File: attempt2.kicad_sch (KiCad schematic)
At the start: 70 parts, among them J1 SIM_Card, J3 U.FL-R-SMT-110, J4 USB_C_Receptacle_USB2.0_14P, J5 U.FL-R-SMT-110, SW3 SW_Push, SW4 SW_Push, U1 nRF9160-SIxA, U3 MCP73831T-2ACI_OT, U4 MIC94092YC6-TR, U7 CP2102N-A02-GQFN24R

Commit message: all the footprints...
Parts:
- BT1: footprint (none) -> PCB_schem_downloads:SEIKO_ML414H_IV01E
- C1, C10, C11, C12, C13, C14, C15, C16, C19, C4, C5, C6, C8, C9: footprint (none) -> Capacitor_SMD:C_1206_3216Metric
- D1, D3: footprint (none) -> LED_SMD:LED_1206_3216Metric
- D4: footprint BAT20JFILM:SOD-323 -> Diode_SMD:D_2114_3652Metric
- J1: footprint (none) -> Connector_Card:nanoSIM_GCT_SIM8060-6-1-14-00
- J3, J5: footprint CONN1_UFL-R_HIR -> footprints:CONN1_UFL-R_HIR
- J4: footprint (none) -> Connector_USB:USB_C_Receptacle_GCT_USB4110
- JP2: footprint (none) -> Jumper:SolderJumper-2_P1.3mm_Open_RoundedPad1.0x1.5mm
- L1, L4: footprint (none) -> Inductor_SMD:L_1206_3216Metric
- PS1: footprint TPS63031DSKR:SON50P250X250X80-11N -> Package_SON:WSON-10-1EP_2.5x2.5mm_P0.5mm_EP1.2x2mm
- R1, R10, R11, R12, R15, R16, R17, R2, R20, R21, R3, R4, R5, R6, R7, R8, R9: footprint (none) -> Resistor_SMD:R_1206_3216Metric
- SW3: footprint (none) -> Button_Switch_SMD:SW_Push_1P1T_NO_CK_PTS125Sx43PSMTR
- SW4: footprint (none) -> Button_Switch_SMD:SW_Push_1P1T_NO_CK_PTS125Sx73SMTR
- TP1, TP10, TP11, TP13, TP14, TP15, TP16, TP19, TP2, TP20, TP21, TP3, TP4, TP5, TP6, TP7, TP8, TP9: footprint (none) -> TestPoint:TestPoint_Pad_D2.0mm
- U3: footprint MCP73831T-2ACI_OT:SOT95P280X145-5N -> MCP73831T_2ACI_OT:SOT95P280X145-5N
- U4: footprint SC-70-6_C6_MCH -> footprints:SC-70-6_C6_MCH
- U7: footprint CP2102N-A02-GQFN24R:QFN50P400X400X80-25N -> CP2102N_A02_GQFN24R:QFN50P400X400X80-25N
- gave numbers to parts that had none: 1
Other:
- note added: "# TODO: ## bake - give mia the battery sense voltage divider values - antennae things ## mia - assign footprints :) all done except for sw pins - add notes about the expected voltage/current values for things (ie. buck/boost output, VBUS/VSYS lines, etc.) - route pcb"
- note added: "VBAT = (2.0, 3.0, 3.1)V 1.0mAh Battery: ML414H IV01E Coin Cell Battery"
- note added: "VBUS = 5.0V +-0.5v 48V DC 280W USB4110-GF-A"
- note added: "VSYS = (3.3, 3.3, 3.3)V VIN RANGE: 1.8-5.5V"
- note removed: "# TODO: ## bake - give mia the battery sense voltage divider values - antennae things ## mia - assign footprints :) - add notes about the expected voltage/current values for things (ie. buck/boost output, VBUS/VSYS lines, etc.) - route pcb"
- note removed: "VBAT = (3.0, 3.7, 4.2)V"
- note removed: "VBUS = 5.1V +-0.5v"

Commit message: started work on pcb
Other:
- note added: "VBAT = (3.0, 3.7, 4.2)V"
- note added: "VBUS = 5.1V +-0.5v"
- note removed: "VBAT = (2.0, 3.0, 3.1)V 1.0mAh Battery: ML414H IV01E Coin Cell Battery"
- note removed: "VBUS = 5.0V +-0.5v 48V DC 280W USB4110-GF-A"
- note removed: "VSYS = (3.3, 3.3, 3.3)V VIN RANGE: 1.8-5.5V"
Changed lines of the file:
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@@
 		)
 	)
-	(text "VBUS = 5.0V +-0.5v 48V DC 280W\nUSB4110-GF-A"
+	(text "VBUS = 5.1V +-0.5v"
 		(exclude_from_sim no)
-		(at 56.896 259.08 0)
+		(at 51.308 253.746 0)
 		(effects
 			(font
@@
 		)
 	)
-	(text "VBAT = (2.0, 3.0, 3.1)V 1.0mAh\nBattery: ML414H IV01E Coin Cell Battery\n"
+	(text "VBAT = (3.0, 3.7, 4.2)V"
 		(exclude_from_sim no)
 		(at 91.186 336.296 0)
@@
 			)
 		)
-	)
-	(text "VSYS = (3.3, 3.3, 3.3)V\nVIN RANGE: 1.8-5.5V\n"
-		(exclude_from_sim no)
-		(at 231.648 287.782 0)
-		(effects
-			(font
-				(size 1.27 1.27)
-			)
-		)

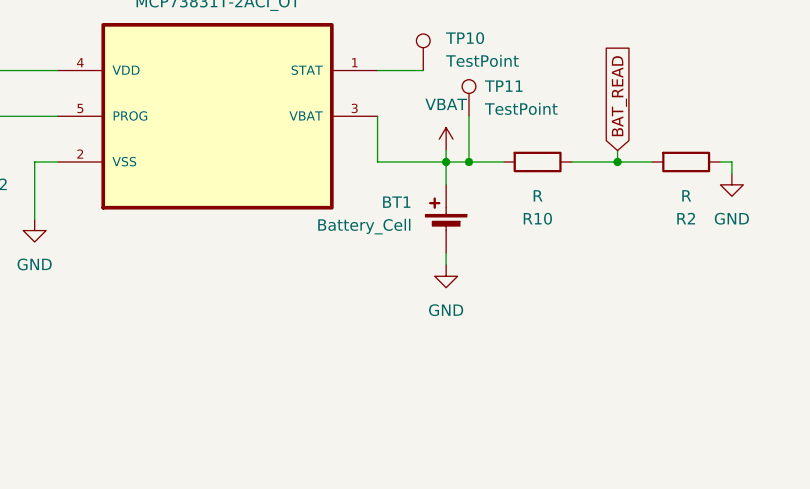
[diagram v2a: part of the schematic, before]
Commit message: added a diode
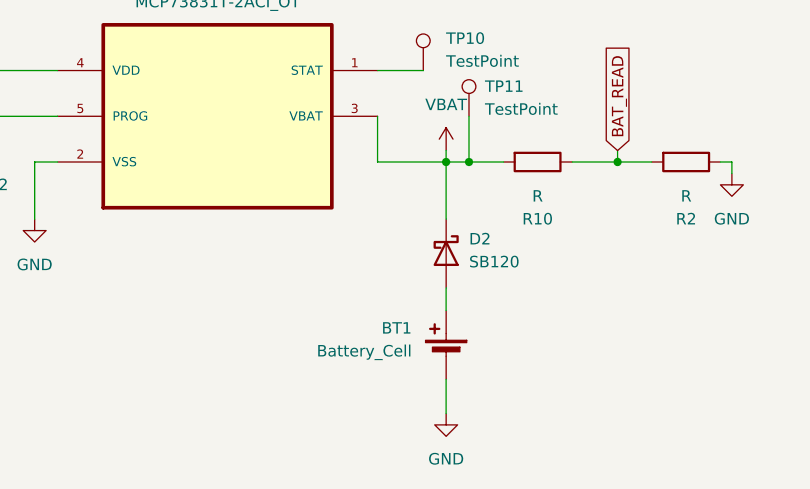
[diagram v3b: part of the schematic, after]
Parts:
- added D2: SB120, Diode_THT:D_DO-41_SOD81_P10.16mm_Horizontal, symbol Diode:SB120
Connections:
- net VBAT: now also D2.1 (K); no longer BT1.1 (+)
- new net: BT1.1 (+), D2.2 (A)
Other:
- moved on the sheet: BT1
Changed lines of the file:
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@@
 	(wire
 		(pts
+			(xy 115.57 373.38) (xy 115.57 367.03)
+		)
+		(stroke
+			(width 0)
+			(type default)
+		)
+	)
+	(wire
+		(pts
 			(xy 252.73 110.49) (xy 276.86 110.49)
 		)
@@
 	(wire
 		(pts
-			(xy 115.57 378.46) (xy 115.57 377.19)
+			(xy 115.57 391.16) (xy 115.57 394.97)
 		)
 		(stroke
@@
 	(wire
 		(pts
-			(xy 115.57 369.57) (xy 115.57 367.03)
+			(xy 115.57 383.54) (xy 115.57 381)
 		)
 		(stroke
@@
 	)
 	(symbol
+		(lib_id "Diode:SB120")
+		(at 115.57 377.19 270)
+		(unit 1)
+		(exclude_from_sim no)
+		(in_bom yes)
+		(on_board yes)
+		(dnp no)
+		(fields_autoplaced yes)
+		(property "Reference" "D2"
+			(at 118.11 375.6024 90)
+			(effects
+				(font
+					(size 1.27 1.27)
+				)
+				(justify left)
+			)
+		)
+		(property "Value" "SB120"
+			(at 118.11 378.1424 90)
+			(effects
+				(font
+					(size 1.27 1.27)
+				)
+				(justify left)
+			)
+		)
+		(property "Footprint" "Diode_THT:D_DO-41_SOD81_P10.16mm_Horizontal"
+			(at 111.125 377.19 0)
+			(effects
+				(font
+					(size 1.27 1.27)
+				)
+				(hide yes)
+			)
+		)
+		(property "Datasheet" "http://www.diodes.com/_files/datasheets/ds23022.pdf"
+			(at 115.57 377.19 0)
+			(effects
+				(font
+					(size 1.27 1.27)
+				)
+				(hide yes)
+			)
+		)
+		(property "Description" "20V 1A Schottky Barrier Rectifier Diode, DO-41"
+			(at 115.57 377.19 0)
+			(effects
+				(font
+					(size 1.27 1.27)
+				)
+				(hide yes)
+			)
+		)
+		(pin "2"
+		)
+		(pin "1"
+		)
+		(instances
+			(project ""
+				(path "/b2ea7ca0-f81a-4f8c-9e17-16fbc56b39ae"
+					(reference "D2")
+					(unit 1)
+				)
+			)
+		)
+	)
+	(symbol
 		(lib_id "Device:L")
 		(at 74.93 62.23 90)
@@
 	(symbol
 		(lib_id "power:GND")
-		(at 115.57 378.46 0)
+		(at 115.57 394.97 0)
 		(unit 1)
 		(exclude_from_sim no)
@@
 		(fields_autoplaced yes)
 		(property "Reference" "#PWR026"
-			(at 115.57 384.81 0)
+			(at 115.57 401.32 0)
 			(effects
 				(font
@@
 		)
 		(property "Value" "GND"
-			(at 115.57 383.54 0)
+			(at 115.57 400.05 0)
 			(effects
 				(font
@@
 		)
 		(property "Footprint" ""
-			(at 115.57 378.46 0)
+			(at 115.57 394.97 0)
 			(effects
 				(font
@@
 		)
 		(property "Datasheet" ""
-			(at 115.57 378.46 0)
+			(at 115.57 394.97 0)
 			(effects
 				(font
@@
 		)
 		(property "Description" "Power symbol creates a global label with name \"GND\" , ground"
-			(at 115.57 378.46 0)
+			(at 115.57 394.97 0)
 			(effects
 				(font
@@
 	(symbol
 		(lib_id "Device:Battery_Cell")
-		(at 115.57 374.65 0)
+		(at 115.57 388.62 0)
 		(mirror y)
 		(unit 1)
@@
 		(dnp no)
 		(property "Reference" "BT1"
-			(at 111.76 371.5384 0)
+			(at 111.76 385.5084 0)
 			(effects
 				(font
@@
 		)
 		(property "Value" "Battery_Cell"
-			(at 111.76 374.0784 0)
+			(at 111.76 388.0484 0)
 			(effects
 				(font
@@
 		)
 		(property "Footprint" "PCB_schem_downloads:SEIKO_ML414H_IV01E"
-			(at 115.57 373.126 90)
+			(at 115.57 387.096 90)
 			(effects
 				(font
@@
 		)
 		(property "Datasheet" "~"
-			(at 115.57 373.126 90)
+			(at 115.57 387.096 90)
 			(effects
 				(font
@@
 		)
 		(property "Description" "Single-cell battery"
-			(at 115.57 374.65 0)
+			(at 115.57 388.62 0)
 			(effects
 				(font

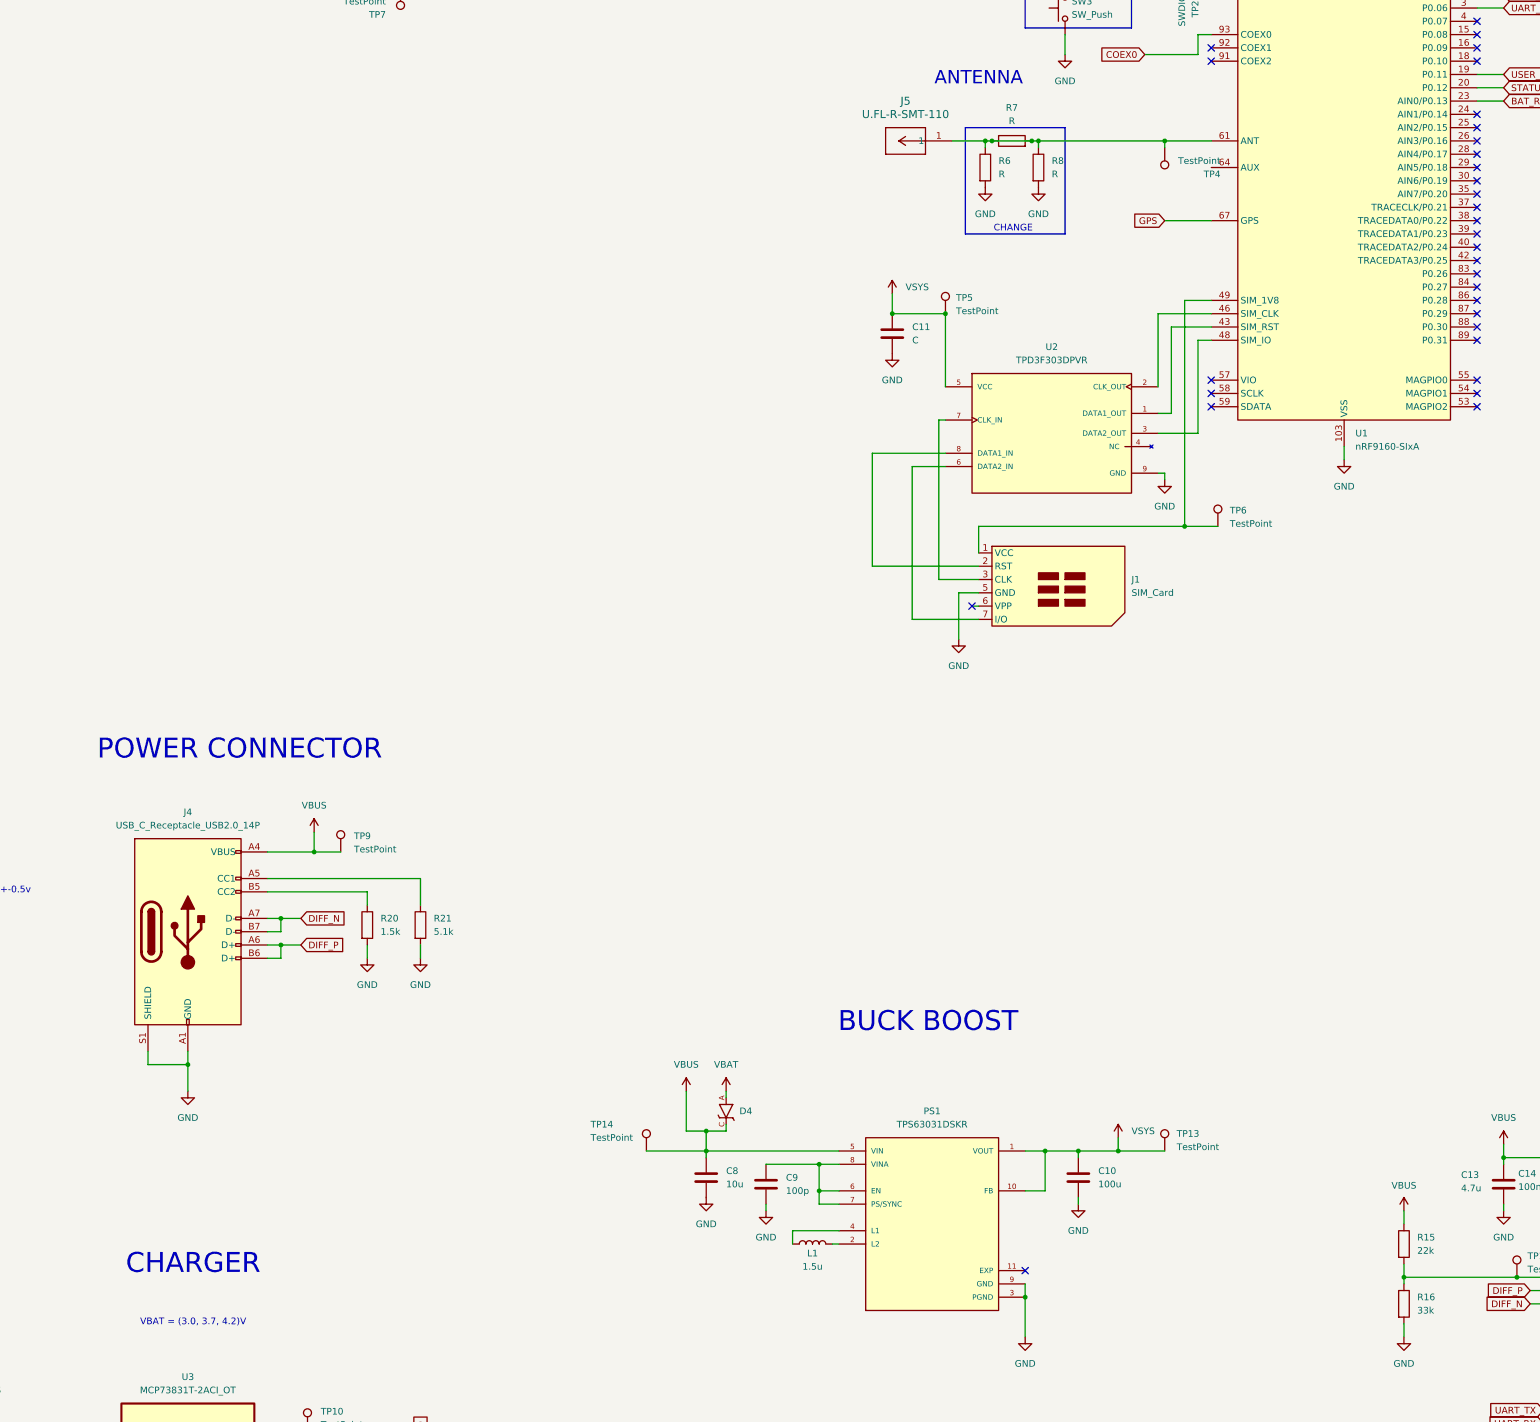
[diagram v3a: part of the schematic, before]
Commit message: changed out antenna and fixed jst battery connector. also edited schematic
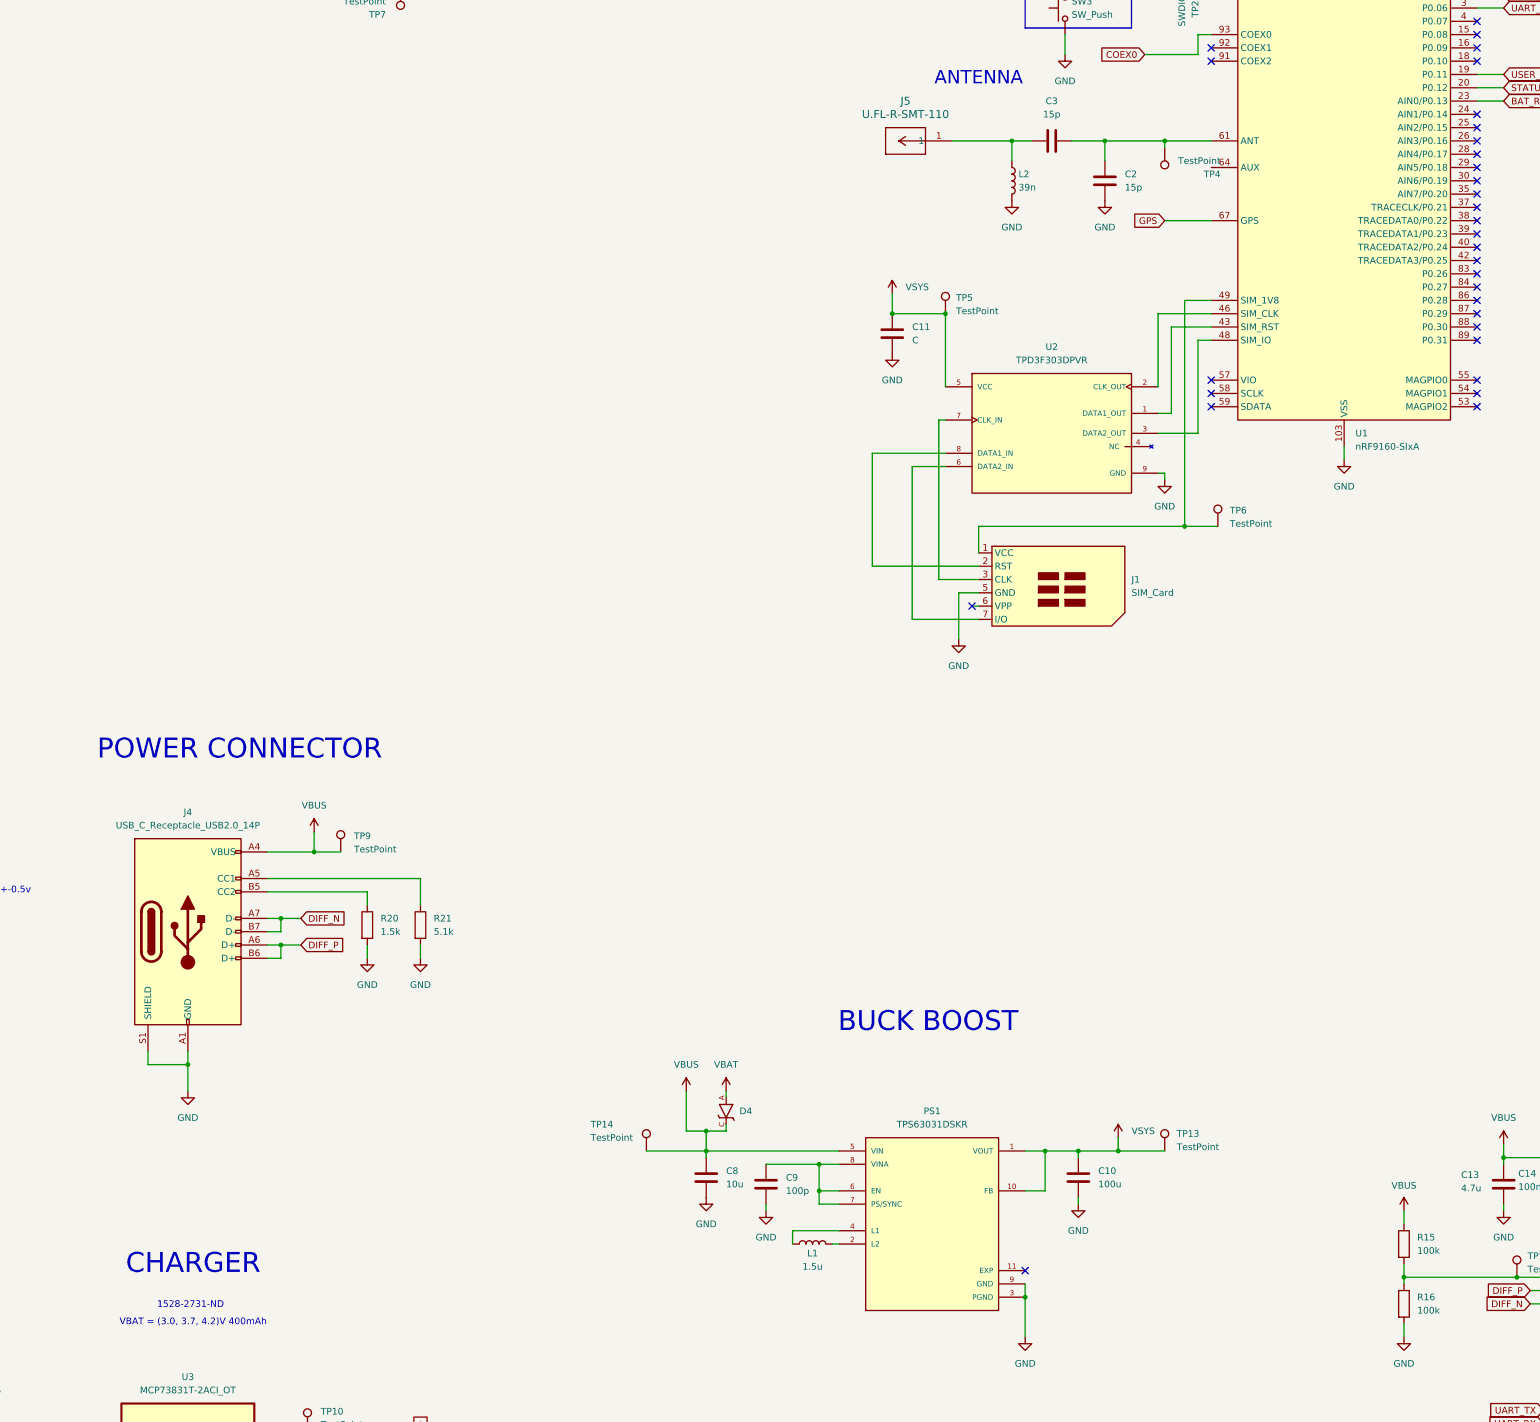
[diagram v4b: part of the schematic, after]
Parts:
- removed R6, R7, R8: R, Resistor_SMD:R_1206_3216Metric, symbol Device:R
- added C2, C3: 15p, Capacitor_SMD:C_1206_3216Metric, symbol Device:C
- added L2: 39n, Inductor_SMD:L_1206_3216Metric, symbol Device:L
- BT1: footprint PCB_schem_downloads:SEIKO_ML414H_IV01E -> Connector_JST:JST_PH_S2B-PH-K_1x02_P2.00mm_Horizontal
- R15: value 22k -> 100k
- R16: value 33k -> 100k
- SW3: footprint Button_Switch_SMD:SW_Push_1P1T_NO_CK_PTS125Sx43PSMTR -> Button_Switch_SMD:SW_Push_1P1T_NO_CK_KMR2
- TP12, TP22: footprint (none) -> TestPoint:TestPoint_Pad_D2.0mm
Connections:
- net GND: now also C2.2, L2.2
- net at TP4.1, U1.61 (ANT): now also C2.1, C3.2; no longer J5.1
- new net: C3.1, J5.1, L2.1
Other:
- note added: "1528-2731-ND"
- note added: "VBAT = (3.0, 3.7, 4.2)V 400mAh"
- note removed: "CHANGE"
- note removed: "VBAT = (3.0, 3.7, 4.2)V"

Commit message: changed the connector to a jst_phr_2
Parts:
- BT1: footprint Connector_JST:JST_PH_S2B-PH-K_1x02_P2.00mm_Horizontal -> PHR_2:JST_PHR-2
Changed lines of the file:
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@@
 			)
 		)
-		(property "Footprint" "Connector_JST:JST_PH_S2B-PH-K_1x02_P2.00mm_Horizontal"
+		(property "Footprint" "PHR_2:JST_PHR-2"
 			(at 115.57 387.096 90)
 			(effects
